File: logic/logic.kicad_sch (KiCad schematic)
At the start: 15 parts, among them J1 DIN41612_03x32_ABC, J2 Conn_02x05_Odd_Even, J3 Conn_02x05_Odd_Even, U1 TPIC6595, U2 TPIC6595, U3 TPIC6595, U4 TPIC6595, U5 TPIC6595, U6 TPIC6595, U7 TPIC6595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

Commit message: Ongoing development of logic board.
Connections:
- net ~{SRCLR3.3}: now also U9.2 (I0a); no longer U9.8 (I3a)
- net at J3.1 (Pin_1): now also RN1.14 (R3.2); no longer RN1.12 (R5.2)
- net at J3.2 (Pin_2): now also RN1.13 (R4.2); no longer RN1.11 (R6.2)
- net at J3.3 (Pin_3): now also RN1.12 (R5.2); no longer RN1.13 (R4.2)
- net at J3.4 (Pin_4): now also RN1.11 (R6.2); no longer RN1.10 (R7.2)
- net at J3.5 (Pin_5): now also RN1.10 (R7.2); no longer RN1.14 (R3.2)
- net at A1.D7: now also U9.8 (I3a); no longer U9.2 (I0a)

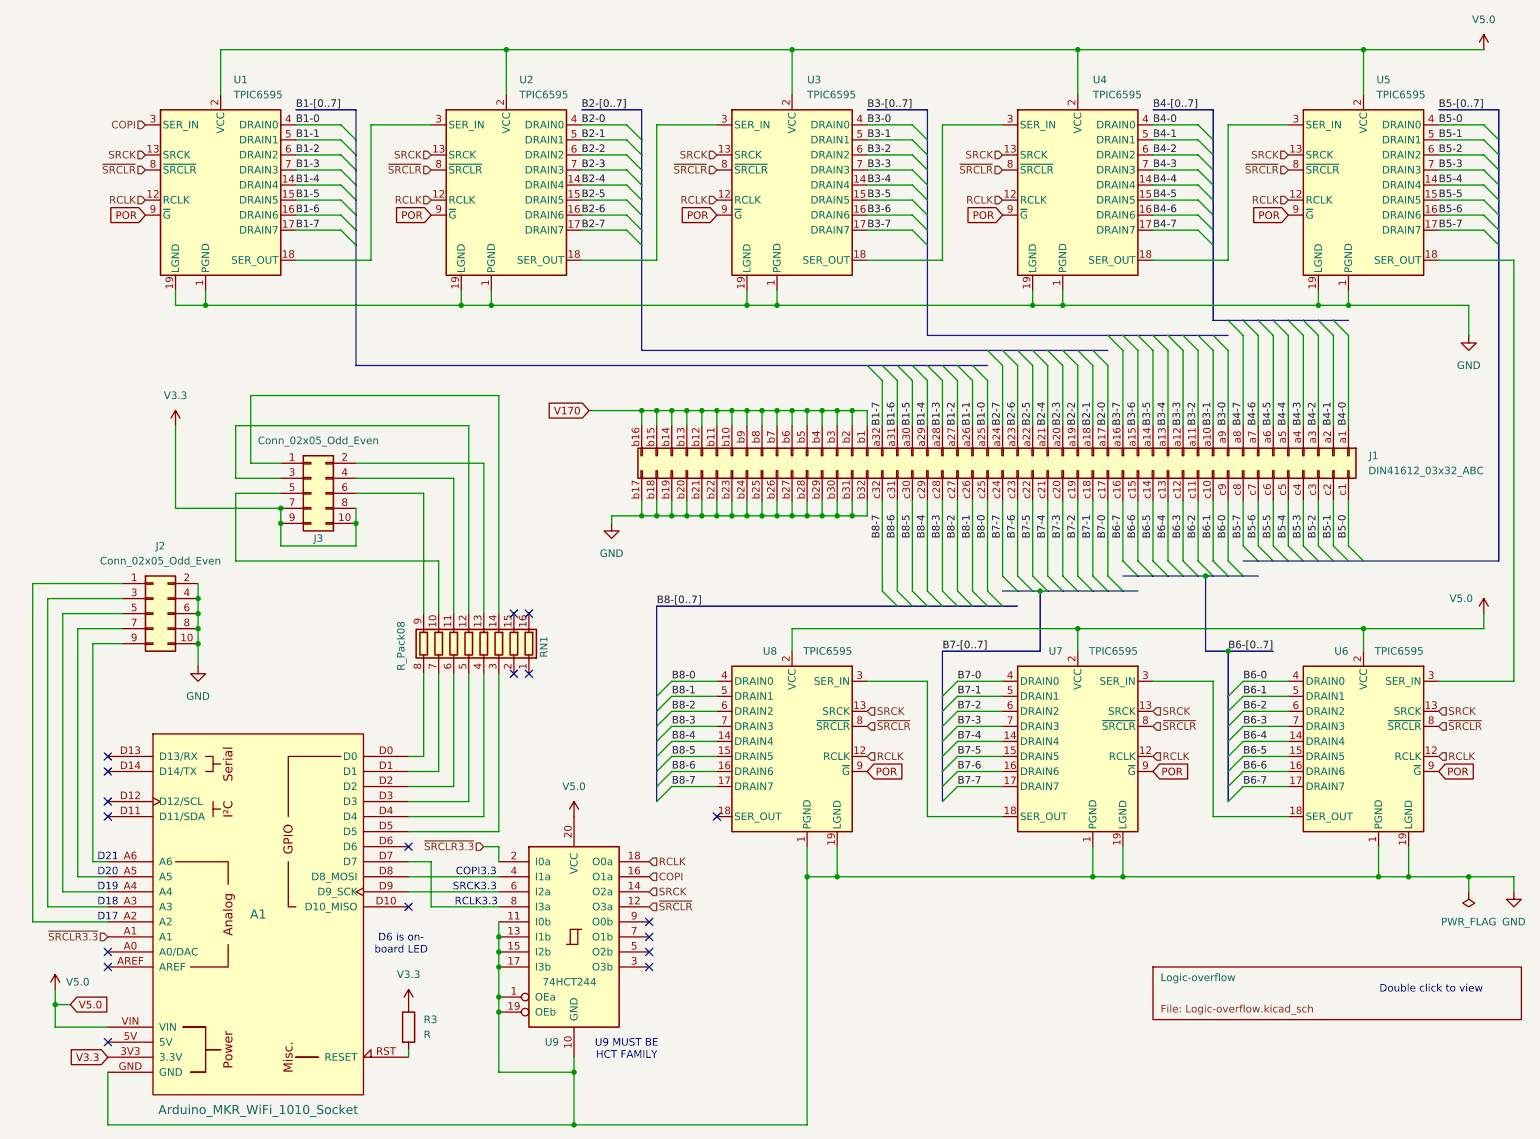
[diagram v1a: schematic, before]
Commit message: Logic board is mostly routed. Changes to schematic for routing.
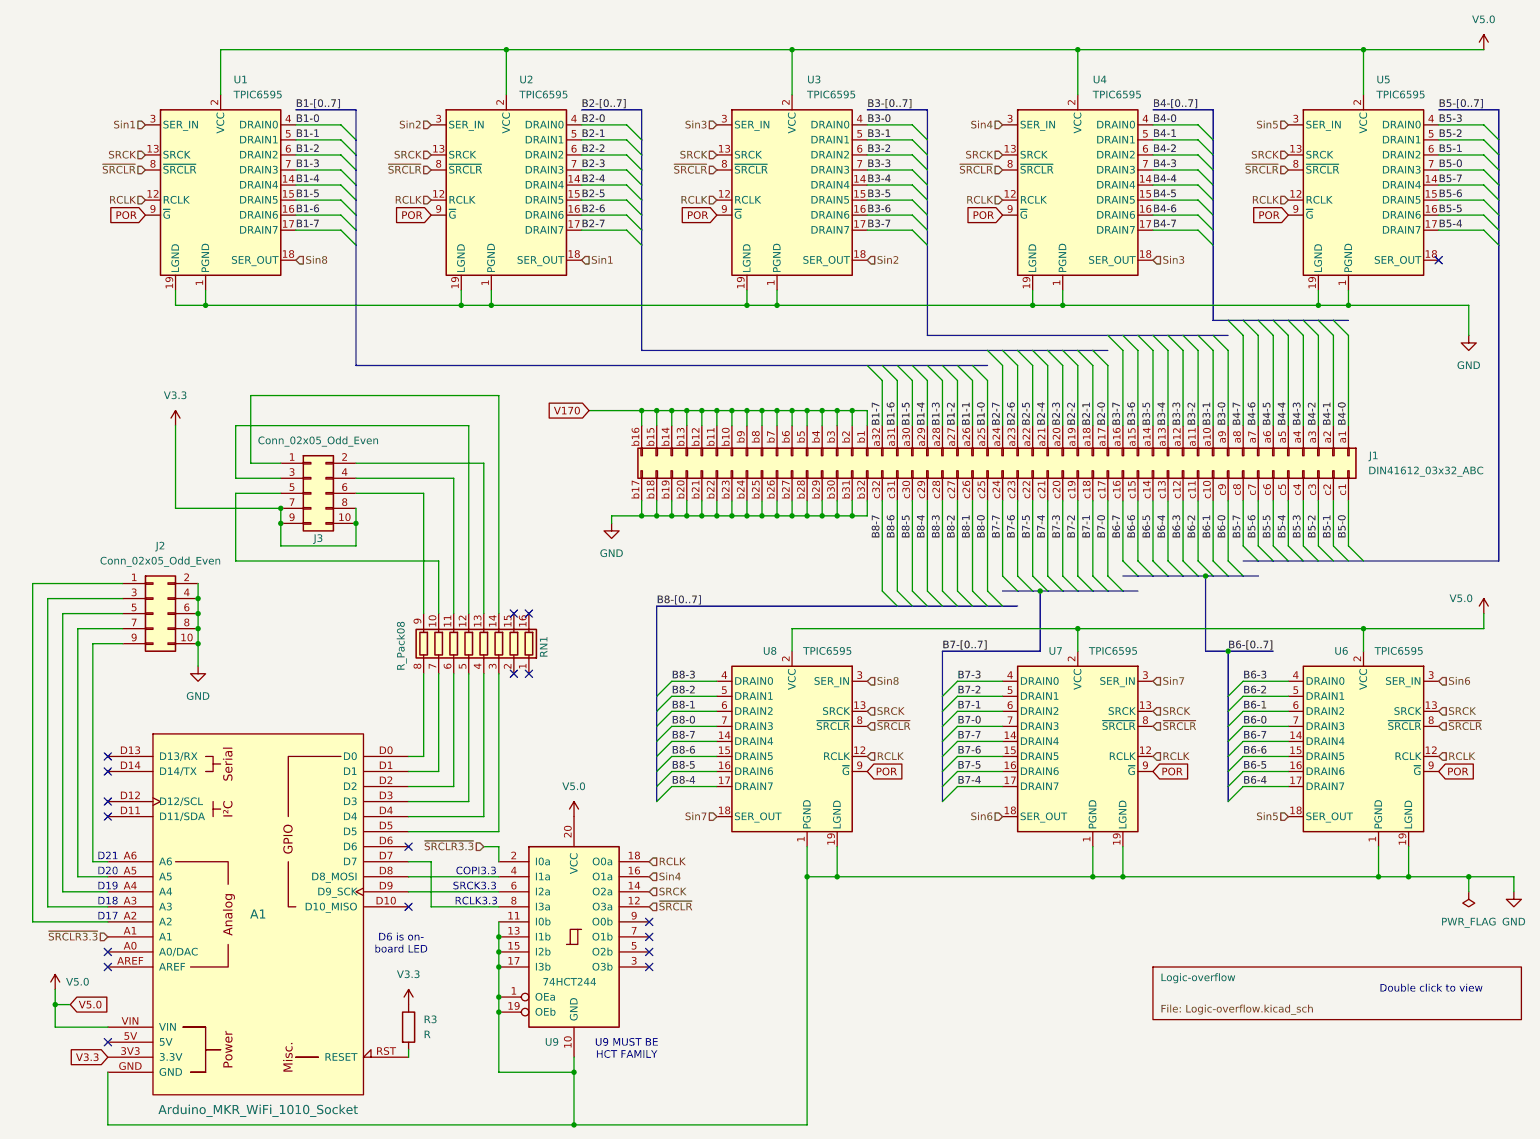
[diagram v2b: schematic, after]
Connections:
- net B5-0: now also U5.7 (DRAIN3); no longer U5.4 (DRAIN0)
- net B5-1: now also U5.6 (DRAIN2); no longer U5.5 (DRAIN1)
- net B5-2: now also U5.5 (DRAIN1); no longer U5.6 (DRAIN2)
- net B5-3: now also U5.4 (DRAIN0); no longer U5.7 (DRAIN3)
- net B5-4: now also U5.17 (DRAIN7); no longer U5.14 (DRAIN4)
- net B5-5: now also U5.16 (DRAIN6); no longer U5.15 (DRAIN5)
- net B5-6: now also U5.15 (DRAIN5); no longer U5.16 (DRAIN6)
- net B5-7: now also U5.14 (DRAIN4); no longer U5.17 (DRAIN7)
- net B6-0: now also U6.7 (DRAIN3); no longer U6.4 (DRAIN0)
- net B6-1: now also U6.6 (DRAIN2); no longer U6.5 (DRAIN1)
- net B6-2: now also U6.5 (DRAIN1); no longer U6.6 (DRAIN2)
- net B6-3: now also U6.4 (DRAIN0); no longer U6.7 (DRAIN3)
- net B6-4: now also U6.17 (DRAIN7); no longer U6.14 (DRAIN4)
- net B6-5: now also U6.16 (DRAIN6); no longer U6.15 (DRAIN5)
- net B6-6: now also U6.15 (DRAIN5); no longer U6.16 (DRAIN6)
- net B6-7: now also U6.14 (DRAIN4); no longer U6.17 (DRAIN7)
- net B7-0: now also U7.7 (DRAIN3); no longer U7.4 (DRAIN0)
- net B7-1: now also U7.6 (DRAIN2); no longer U7.5 (DRAIN1)
- net B7-2: now also U7.5 (DRAIN1); no longer U7.6 (DRAIN2)
- net B7-3: now also U7.4 (DRAIN0); no longer U7.7 (DRAIN3)
- net B7-4: now also U7.17 (DRAIN7); no longer U7.14 (DRAIN4)
- net B7-5: now also U7.16 (DRAIN6); no longer U7.15 (DRAIN5)
- net B7-6: now also U7.15 (DRAIN5); no longer U7.16 (DRAIN6)
- net B7-7: now also U7.14 (DRAIN4); no longer U7.17 (DRAIN7)
- net B8-0: now also U8.7 (DRAIN3); no longer U8.4 (DRAIN0)
- net B8-1: now also U8.6 (DRAIN2); no longer U8.5 (DRAIN1)
- net B8-2: now also U8.5 (DRAIN1); no longer U8.6 (DRAIN2)
- net B8-3: now also U8.4 (DRAIN0); no longer U8.7 (DRAIN3)
- net B8-4: now also U8.17 (DRAIN7); no longer U8.14 (DRAIN4)
- net B8-5: now also U8.16 (DRAIN6); no longer U8.15 (DRAIN5)
- net B8-6: now also U8.15 (DRAIN5); no longer U8.16 (DRAIN6)
- net B8-7: now also U8.14 (DRAIN4); no longer U8.17 (DRAIN7)
- net Sin2: now reaches U3.18 (SER_OUT)
- net Sin2: now also U2.3 (SER_IN); no longer U4.3 (SER_IN)
- net Sin1: now reaches U2.18 (SER_OUT)
- net Sin1: now also U1.3 (SER_IN); no longer U3.3 (SER_IN)
- net Sin8: now reaches U1.18 (SER_OUT)
- net Sin8: now also U8.3 (SER_IN); no longer U2.3 (SER_IN)
- net Sin7: now reaches U8.18 (SER_OUT)
- net Sin7: now also U7.3 (SER_IN)
- net Sin6: now reaches U7.18 (SER_OUT)
- net Sin6: now also U6.3 (SER_IN); no longer U8.3 (SER_IN)
- net at U5.18 (SER_OUT): no longer U6.3 (SER_IN)
- net Sin3: now reaches U4.18 (SER_OUT)
- net Sin3: now also U3.3 (SER_IN); no longer U5.3 (SER_IN)
- net Sin5: now reaches U6.18 (SER_OUT)
- net Sin5: now also U5.3 (SER_IN); no longer U7.3 (SER_IN)
- net COPI renamed Sin4
- net Sin4: now also U4.3 (SER_IN); no longer U1.3 (SER_IN)
